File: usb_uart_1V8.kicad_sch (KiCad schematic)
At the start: 25 parts, among them J1 USB_B_Micro, J2 PZ254V-11-04P, J3 PZ254V-11-04P, Q1 MMBT3904, U1 FT232RNL, U2 TXU0202DCU

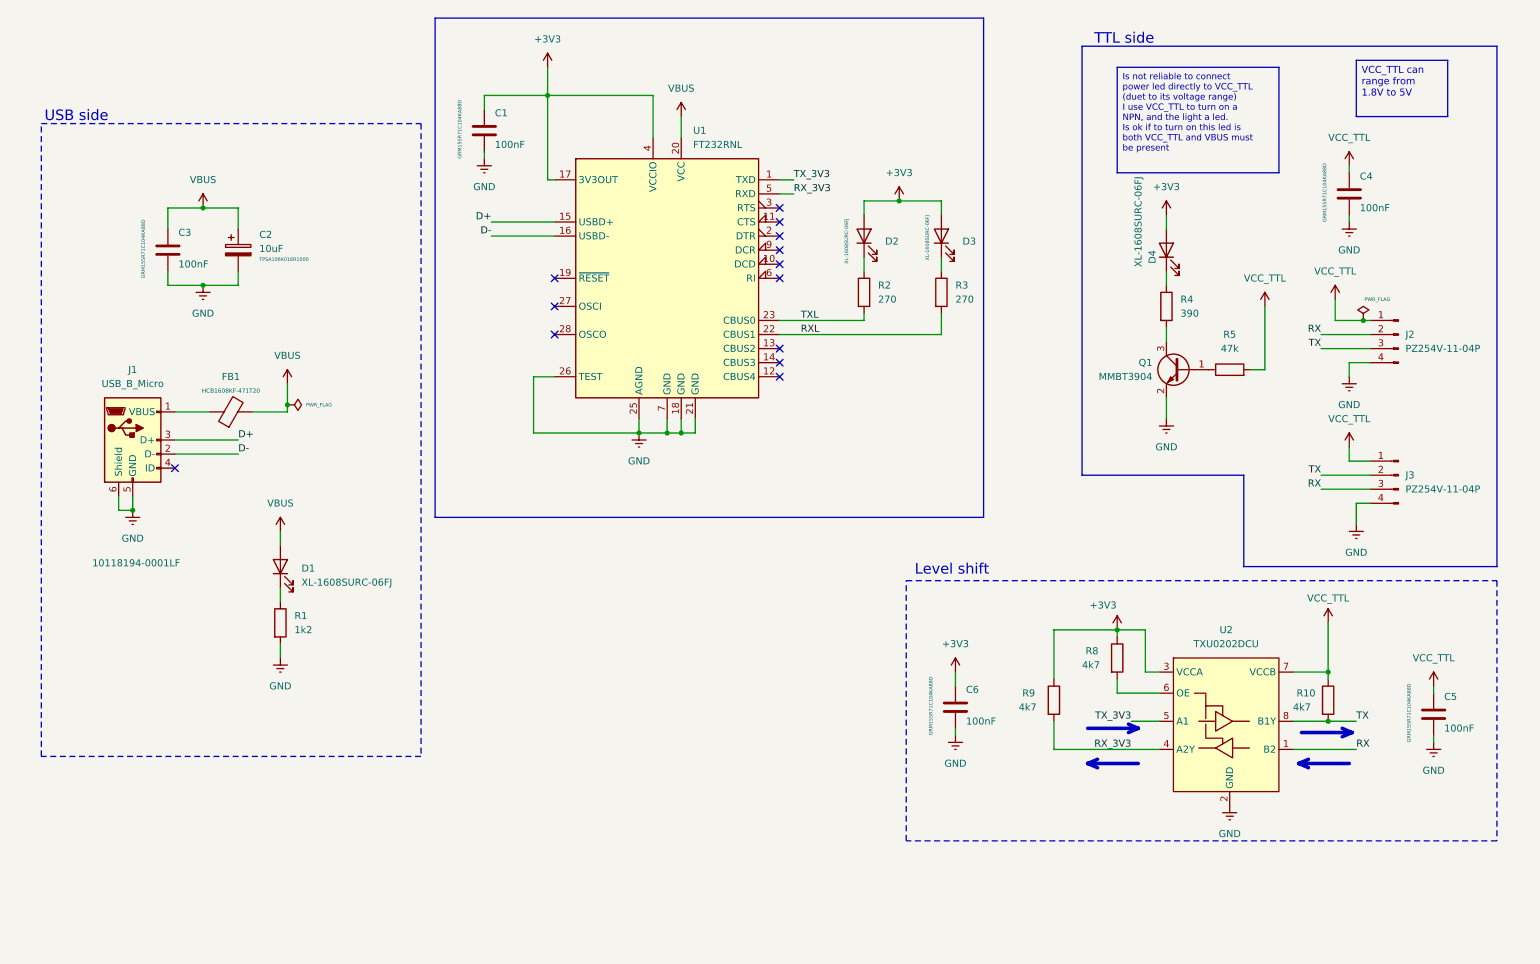
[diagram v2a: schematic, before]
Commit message: [UPG] ver 0.4
- changed some values
- PN basic from JLCPCB
- reduced dimension
- changed some components, now are bigger, eg. 0402 -> 0603
- used handsolder footprint for fome resistor
- changed led (less efficient)
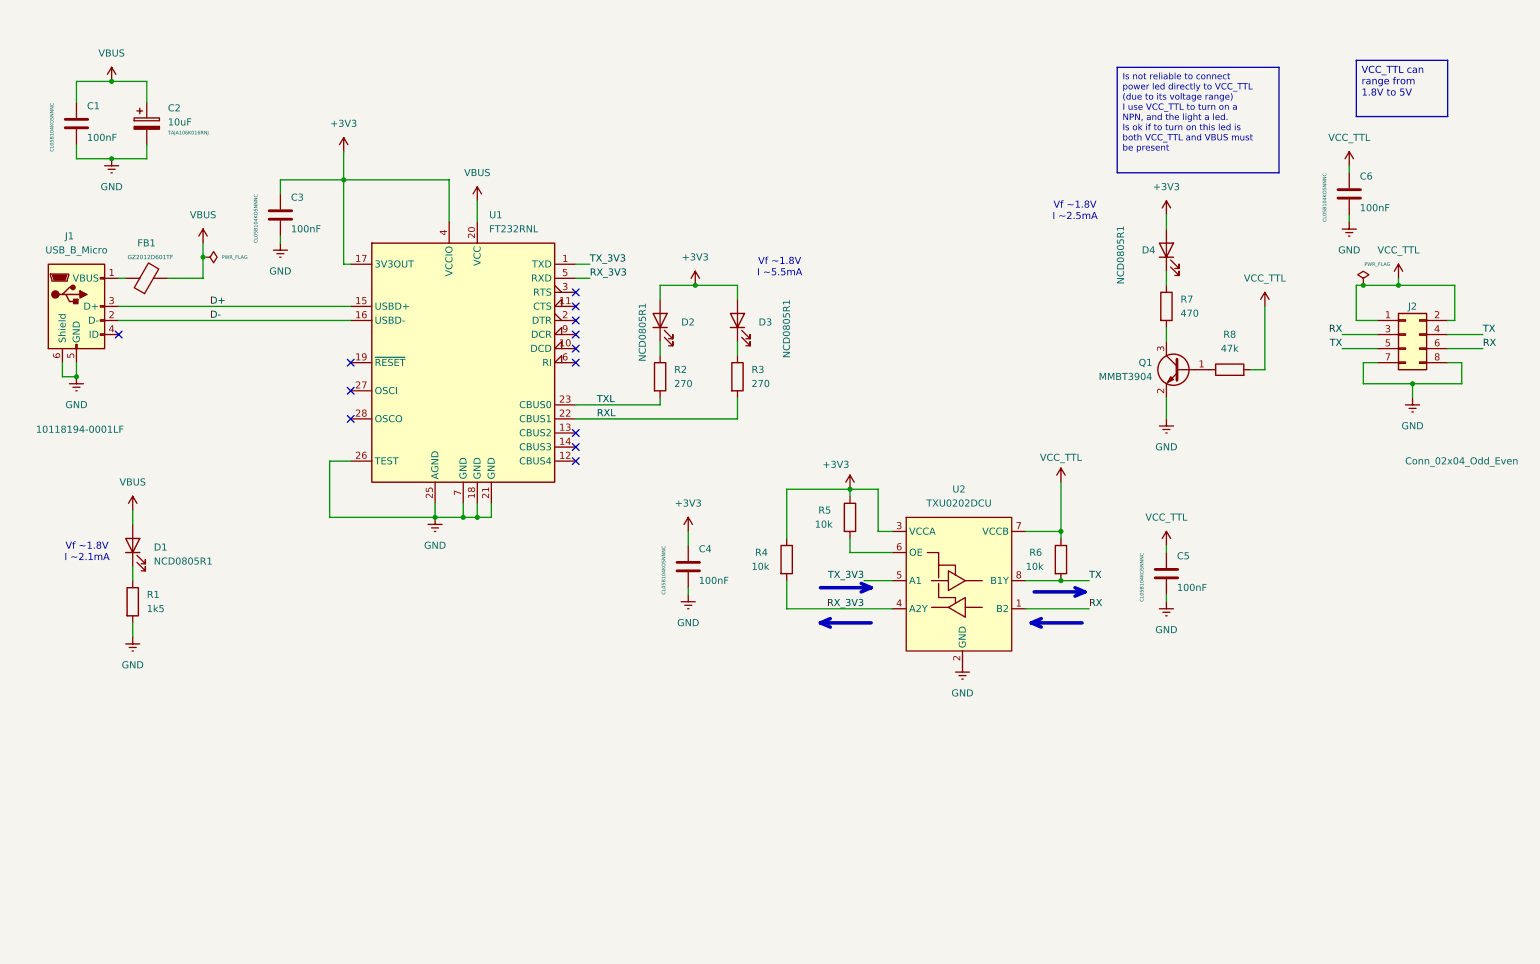
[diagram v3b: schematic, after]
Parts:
- removed C1: 100nF, Capacitor_SMD:C_0402_1005Metric, symbol Device:C
- removed J2, J3: PZ254V-11-04P, Connector_PinHeader_2.54mm:PinHeader_1x04_P2.54mm_Vertical, symbol Connector:Conn_01x04_Pin
- removed R10, R8: 4k7, Resistor_SMD:R_0402_1005Metric, symbol Device:R
- added C3: 100nF, Capacitor_SMD:C_0402_1005Metric, symbol Device:C
- added J2: Conn_02x04_Odd_Even, Connector_PinHeader_2.54mm:PinHeader_2x04_P2.54mm_Vertical, symbol Connector_Generic:Conn_02x04_Odd_Even
- added R5, R6: 10k, Resistor_SMD:R_0402_1005Metric_Pad0.72x0.64mm_HandSolder, symbol Device:R
- C1: renamed from C3; JLCPCB Part# C71629 -> C1525; LCSC C71629 -> C1525
- C2: Field6 TPSA106K016R1000 -> TAJA106K016RNJ; JLCPCB Part# C282116 -> C7171; LCSC C282116 -> C7171
- C4, C5, C6: JLCPCB Part# C71629 -> C1525; LCSC C71629 -> C1525
- D1, D2, D3, D4: value XL-1608SURC-06FJ -> NCD0805R1; footprint LED_SMD:LED_0603_1608Metric -> LED_SMD:LED_0805_2012Metric; JLC 0603 -> 0805; JLCPCB Part# C7371900 -> C84256; LCSC C7371900 -> C84256
- FB1: value HCB1608KF-471T20 -> GZ2012D601TF; JLC 0603 -> 0805; JLCPCB Part# C356977 -> C1017; LCSC C356977 -> C1017
- Q1: JLCPCB Part# C7420353 -> C20526; LCSC C7420353 -> C20526
- R1: value 1k2 -> 1k5; footprint Resistor_SMD:R_0402_1005Metric -> Resistor_SMD:R_0603_1608Metric_Pad0.98x0.95mm_HandSolder; Field6 0402WGF1201TCE -> 0603WAF1501T5E; JLC 0402 -> 0603; JLCPCB Part# C25862 -> C22843; LCSC C25862 -> C22843
- R2, R3: footprint Resistor_SMD:R_0402_1005Metric -> Resistor_SMD:R_0603_1608Metric_Pad0.98x0.95mm_HandSolder; Field6 0402WGF2700TCE -> 0603WAF2700T5E; JLC 0402 -> 0603; JLCPCB Part# C25099 -> C22966; LCSC C25099 -> C22966
- R4: renamed from R9; value 4k7 -> 10k; footprint Resistor_SMD:R_0402_1005Metric -> Resistor_SMD:R_0402_1005Metric_Pad0.72x0.64mm_HandSolder; Field6 0402WGF4701TCE -> 0402WGF1002TCE; JLCPCB Part# C25900 -> C25744; LCSC C25900 -> C25744
- R7: renamed from R4; value 390 -> 470; footprint Resistor_SMD:R_0402_1005Metric -> Resistor_SMD:R_0603_1608Metric_Pad0.98x0.95mm_HandSolder; Field6 0402WGJ0391TCE -> 0603WAF4700T5E; JLC 0402 -> 0603; JLCPCB Part# C25163 -> C23179; LCSC C25163 -> C23179
- R8: renamed from R5; footprint Resistor_SMD:R_0402_1005Metric -> Resistor_SMD:R_0603_1608Metric_Pad0.98x0.95mm_HandSolder; Field6 0402WGF4702TCE -> 0603WAF4702T5E; JLC 0402 -> 0603; JLCPCB Part# C25792 -> C25819; LCSC C25792 -> C25819
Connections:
- net +3V3: now also C4.1, C3.1, R5.1; no longer C6.1
- net GND: now also C3.2, J2.7 (Pin_7), J2.8 (Pin_8)
- net RX: now also J2.3 (Pin_3), J2.6 (Pin_6)
- net TX: now also J2.4 (Pin_4), J2.5 (Pin_5), R6.2
- net VCC_TTL: now also C6.1, J2.1 (Pin_1), J2.2 (Pin_2), R6.1; no longer C4.1
- net at U2.6 (OE): now also R5.2
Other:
- note added: "Vf ~1.8V I ~2.1mA"
- note added: "Vf ~1.8V I ~2.5mA"
- note added: "Vf ~1.8V I ~5.5mA"
- note removed: "Level shift"
- note removed: "TTL side"
- note removed: "USB side"
- moved on the sheet: C1, C2, D1, FB1, J1, R1, R2, R4, U1, U2

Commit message: [UPG] changed connector from micro-b to usb-c
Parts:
- removed J1: USB_B_Micro, Connector_USB:USB_Micro-B_Amphenol_10118194-0001LF_Horizontal, symbol Connector:USB_B_Micro
- added J1: USB_C_Receptacle_USB2.0_16P, Connector_USB:USB_C_Receptacle_GCT_USB4105-xx-A_16P_TopMnt_Horizontal, symbol Connector:USB_C_Receptacle_USB2.0_16P
- added R10, R9: 5k1, Capacitor_SMD:C_0402_1005Metric_Pad0.74x0.62mm_HandSolder, symbol Device:R_Small
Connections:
- net D+: now also J1.A6 (D+), J1.B6 (D+)
- net D-: now also J1.A7 (D-), J1.B7 (D-)
- net GND: now also J1.A1 (GND), J1.A12 (GND), J1.B1 (GND), J1.B12 (GND), J1.S1 (SHIELD), R10.2, R9.2
- net at FB1.1: now also J1.A4 (VBUS), J1.A9 (VBUS), J1.B4 (VBUS), J1.B9 (VBUS)
- new net: J1.B5 (CC2), R10.1
- new net: J1.A5 (CC1), R9.1
- no-connect marks 13 -> 14
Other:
- moved on the sheet: C3, D1, D2, D3, R1, R2, R3, U1
